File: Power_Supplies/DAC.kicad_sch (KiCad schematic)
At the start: 45 parts, among them J1 Line Out, J2 Headphone Out, U5 TPA6110A2DGN, U7 PCM1780, U8 OPA2134, U9 MAX1044

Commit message: Added ADC schematic
yes
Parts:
- J1, J2: footprint (none) -> Connector_Audio:Jack_3.5mm_CUI_SJ-3523-SMT_Horizontal
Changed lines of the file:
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@@
 			)
 		)
-		(property "Footprint" ""
+		(property "Footprint" "Connector_Audio:Jack_3.5mm_CUI_SJ-3523-SMT_Horizontal"
 			(at 232.41 115.57 0)
 			(effects
@@
 			)
 		)
-		(property "Footprint" ""
+		(property "Footprint" "Connector_Audio:Jack_3.5mm_CUI_SJ-3523-SMT_Horizontal"
 			(at 232.41 102.87 0)
 			(effects

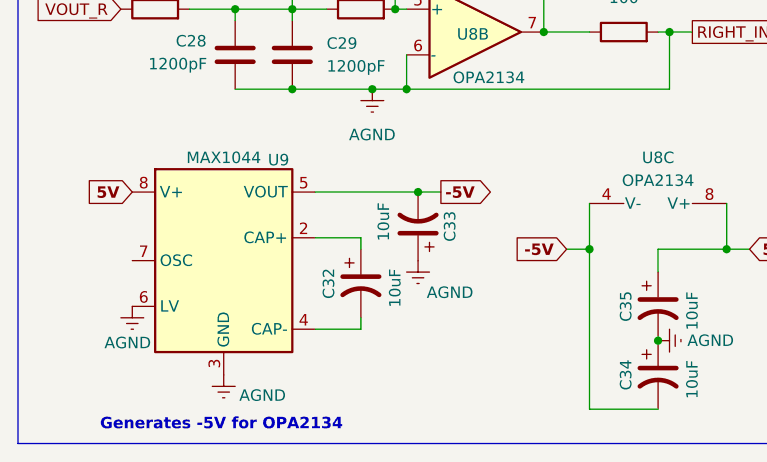
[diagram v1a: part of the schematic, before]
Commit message: Added Phantom Power, updated Xcore library things
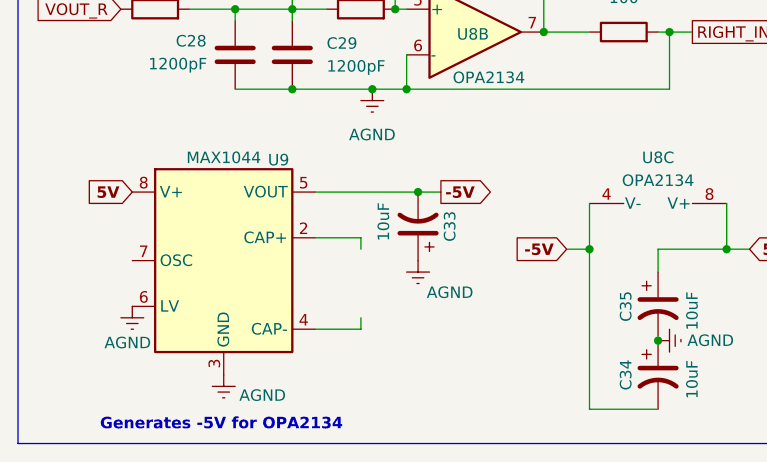
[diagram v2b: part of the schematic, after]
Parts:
- removed C32: 10uF, Capacitor_SMD:CP_Elec_4x5.8, symbol Device:C_Polarized_US
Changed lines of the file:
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@@
-	)
-	(symbol
-		(lib_id "Device:C_Polarized_US")
-		(at 53.34 177.8 0)
-		(unit 1)
-		(exclude_from_sim no)
-		(in_bom yes)
-		(on_board yes)
-		(dnp no)
-		(property "Reference" "C32"
-			(at 49.784 177.8 90)
-			(effects
-				(font
-					(size 1.27 1.27)
-				)
-			)
-		)
-		(property "Value" "10uF"
-			(at 57.15 178.308 90)
-			(effects
-				(font
-					(size 1.27 1.27)
-				)
-			)
-		)
-		(property "Footprint" "Capacitor_SMD:CP_Elec_4x5.8"
-			(at 53.34 177.8 0)
-			(effects
-				(font
-					(size 1.27 1.27)
-				)
-				(hide yes)
-			)
-		)
-		(property "Datasheet" "~"
-			(at 53.34 177.8 0)
-			(effects
-				(font
-					(size 1.27 1.27)
-				)
-				(hide yes)
-			)
-		)
-		(property "Description" "Polarized capacitor, US symbol"
-			(at 53.34 177.8 0)
-			(effects
-				(font
-					(size 1.27 1.27)
-				)
-				(hide yes)
-			)
-		)
-		(pin "1"
-		)
-		(pin "2"
-		)
-		(instances
-			(project "Power_Supplies"
-				(path "/5266cf9e-da90-4c53-80fd-cf3dbed42632/29bf6371-8a12-4a95-b0c2-fbe02aad04a0"
-					(reference "C32")
-					(unit 1)
-				)
-			)
-		)
 	)
 	(symbol

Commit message: Add files via upload
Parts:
- added C140: 10uF, Capacitor_SMD:CP_Elec_4x5.8, symbol Device:C_Polarized_US
- U9: footprint (none) -> SamacSys_Parts:SOIC127P600X175-8N
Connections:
- net at U9.2 (CAP+): now also C140.1
- net at U9.4 (CAP-): now also C140.2
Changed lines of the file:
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@@
 	(symbol
 		(lib_id "Device:C_Polarized_US")
+		(at 53.34 177.8 0)
+		(unit 1)
+		(exclude_from_sim no)
+		(in_bom yes)
+		(on_board yes)
+		(dnp no)
+		(property "Reference" "C140"
+			(at 49.784 177.8 90)
+			(effects
+				(font
+					(size 1.27 1.27)
+				)
+			)
+		)
+		(property "Value" "10uF"
+			(at 57.15 178.308 90)
+			(effects
+				(font
+					(size 1.27 1.27)
+				)
+			)
+		)
+		(property "Footprint" "Capacitor_SMD:CP_Elec_4x5.8"
+			(at 53.34 177.8 0)
+			(effects
+				(font
+					(size 1.27 1.27)
+				)
+				(hide yes)
+			)
+		)
+		(property "Datasheet" "~"
+			(at 53.34 177.8 0)
+			(effects
+				(font
+					(size 1.27 1.27)
+				)
+				(hide yes)
+			)
+		)
+		(property "Description" "Polarized capacitor, US symbol"
+			(at 53.34 177.8 0)
+			(effects
+				(font
+					(size 1.27 1.27)
+				)
+				(hide yes)
+			)
+		)
+		(pin "1"
+		)
+		(pin "2"
+		)
+		(instances
+			(project "Power_Supplies"
+				(path "/5266cf9e-da90-4c53-80fd-cf3dbed42632/29bf6371-8a12-4a95-b0c2-fbe02aad04a0"
+					(reference "C140")
+					(unit 1)
+				)
+			)
+		)
+	)
+	(symbol
+		(lib_id "Device:C_Polarized_US")
 		(at 86.36 187.96 0)
 		(unit 1)
@@
 			)
 		)
-		(property "Footprint" ""
+		(property "Footprint" "SamacSys_Parts:SOIC127P600X175-8N"
 			(at 40.64 177.8 0)
 			(effects

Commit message: Add files via upload
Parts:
- removed C140, C33: 10uF, Capacitor_SMD:CP_Elec_4x5.8, symbol Device:C_Polarized_US
- removed U9: MAX1044, SamacSys_Parts:SOIC127P600X175-8N, symbol Regulator_SwitchedCapacitor:MAX1044
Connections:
- net -5V renamed -5V_2
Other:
- note added: "-5V supply rail for OPA2134 generated by the LT27761 in the ADCs page"
- note removed: "Generates -5V for OPA2134"

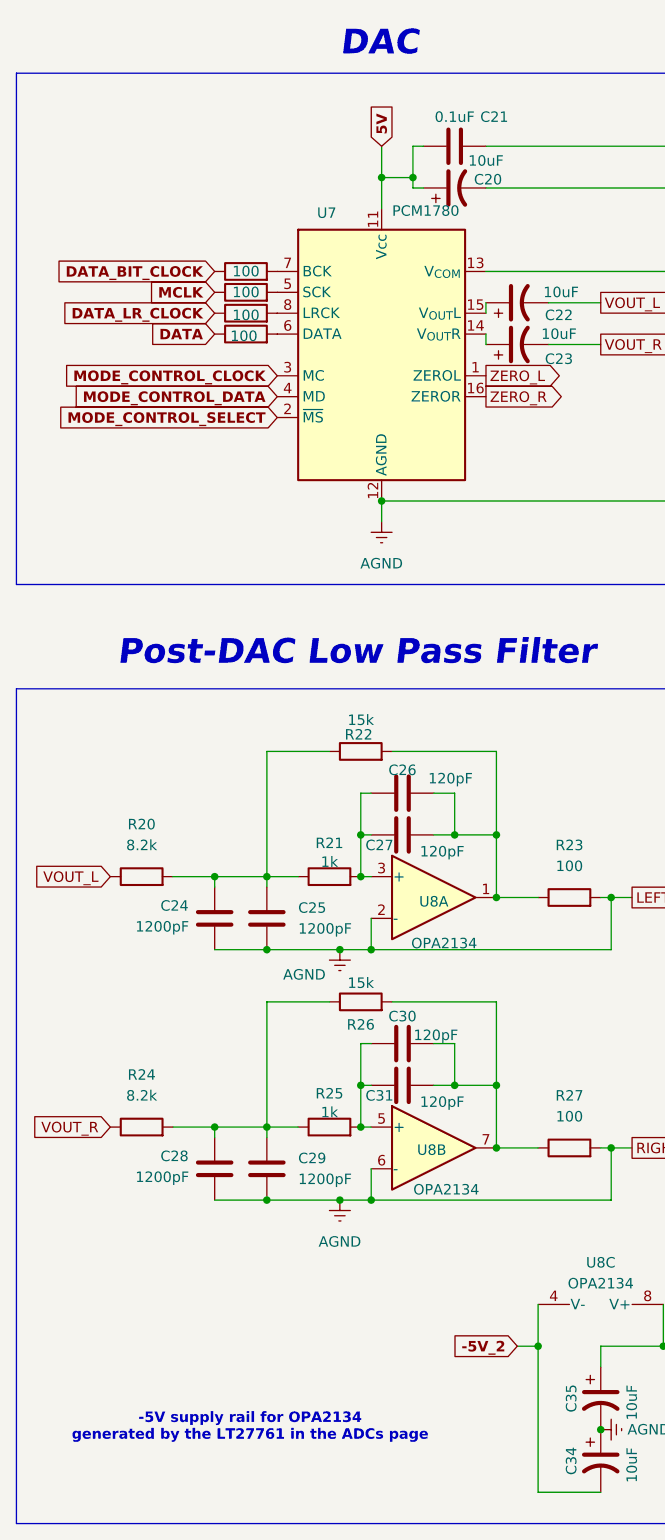
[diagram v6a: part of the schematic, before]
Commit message: Added 3.3V/1.8V LDO, clock IC
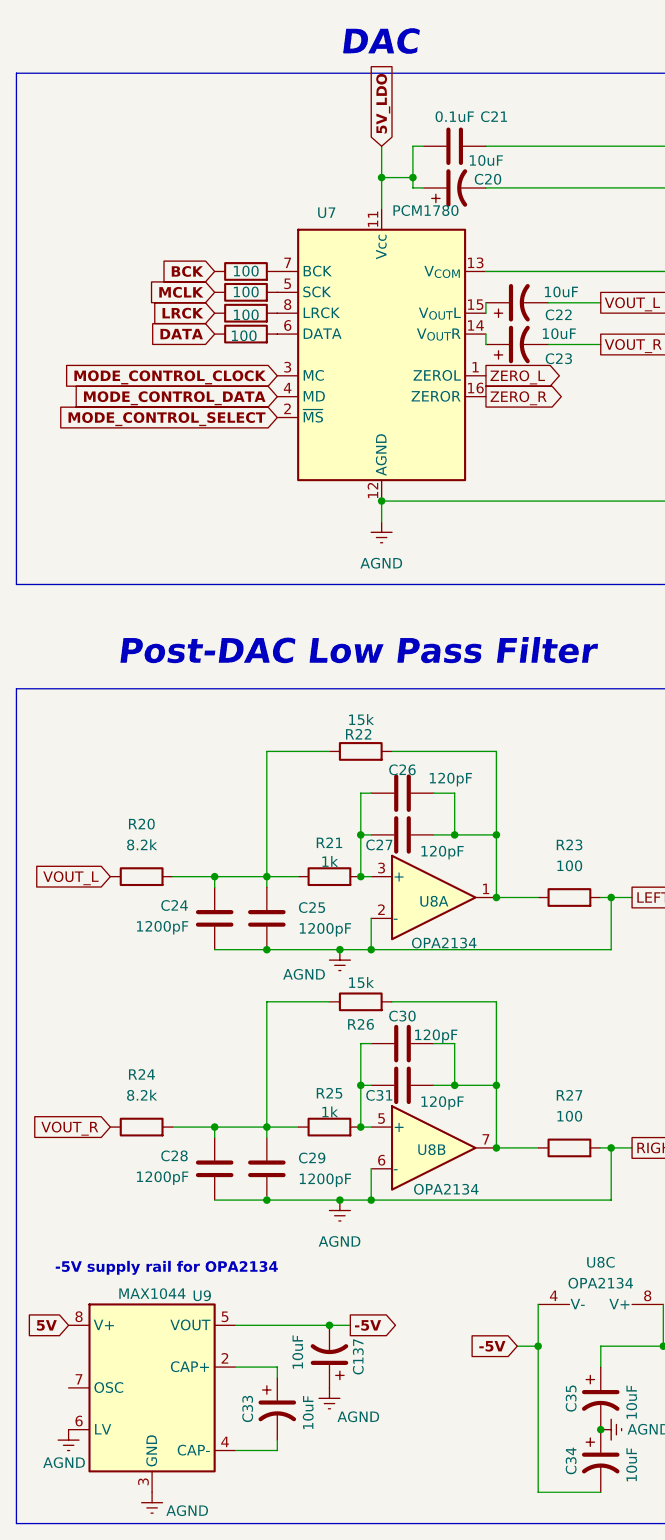
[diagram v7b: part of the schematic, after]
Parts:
- added C137, C33: 10uF, Capacitor_SMD:CP_Elec_4x5.8, symbol Device:C_Polarized_US
- added U9: MAX1044, SamacSys_Parts:SOIC127P600X175-8N, symbol Regulator_SwitchedCapacitor:MAX1044
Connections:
- net 5V: now also U9.8 (V+); no longer C20.1, C21.1, U7.11 (Vcc)
- net AGND: now also C137.1, U9.3 (GND), U9.6 (LV)
- net -5V_2 renamed -5V
- net -5V: now also C137.2, U9.5 (VOUT)
- net DATA_BIT_CLOCK renamed BCK
- net DATA_LR_CLOCK renamed LRCK
- new net: C33.1, U9.2 (CAP+)
- new net: C33.2, U9.4 (CAP-)
- new net 5V_LDO: C20.1, C21.1, U7.11 (Vcc)
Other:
- note added: "-5V supply rail for OPA2134"
- note removed: "-5V supply rail for OPA2134 generated by the LT27761 in the ADCs page"

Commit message: big things are coming...
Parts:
- removed C137, C33: 10uF, Capacitor_SMD:CP_Elec_4x5.8, symbol Device:C_Polarized_US
- removed unit 1 of U8
- removed unit 2 of U8
- removed U9: MAX1044, SamacSys_Parts:SOIC127P600X175-8N, symbol Regulator_SwitchedCapacitor:MAX1044
- added unit 2 of U10
- added unit 1 of U10
- renumbered C24 to C29, C28 to C30, C25 to C31, C29 to C32, C26 to C33, C27 to C34, C30 to C35, C31 to C36, C21 to C37, C20 to C38, C22 to C39, C23 to C40, C35 to C41, C34 to C42, C19 to C43, C12 to C44, C13 to C45, C9 to C46, C10 to C47, C11 to C48, R20 to R17, R24 to R18, R16 to R20, R17 to R21, R18 to R22, R21 to R23, R25 to R24, R22 to R25, R23 to R27, R27 to R28, R12 to R29, R14 to R30, R11 to R31, R15 to R32, R13 to R33, U8 to U10, U5 to U11, U7 to U9
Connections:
- net AGND: now also U10.3 (+), U10.5 (+); no longer C44.1, C45.1, J1.R, J1.T, R27.2, R28.2
- net at C35.1, C36.1, R24.2: now also U10.6 (-)
- net at C33.1, C34.1, R23.2: now also U10.2 (-)
- net at C33.2, C34.2, R25.2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: now also U10.1
- net at C35.2, C36.2, R26.2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: now also U10.7
- new net LEFT_IN: C44.1, J1.T, R27.2
- new net RIGHT_IN: C45.1, J1.R, R28.2
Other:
- note added: "-5V supply rail for OPA2134 shown in ADC Page"
- note removed: "-5V supply rail for OPA2134"
